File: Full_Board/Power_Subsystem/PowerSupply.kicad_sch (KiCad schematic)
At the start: 26 parts, among them IC4 LM2576HVS-5.0_NOPB, J7 KLDHCX-8-0202-A, U1 LM2576SX-3.3-NOPB

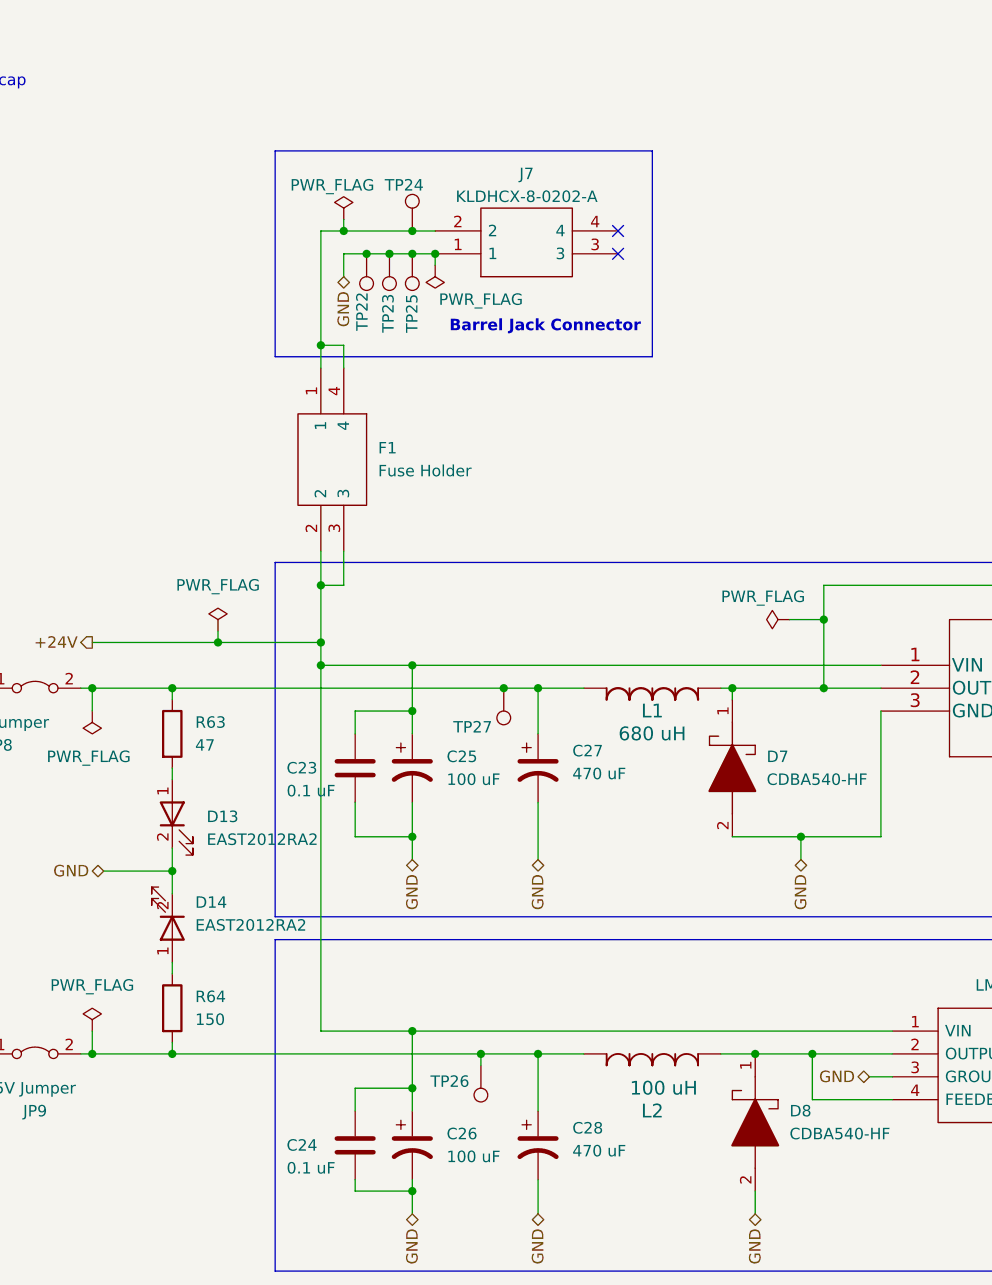
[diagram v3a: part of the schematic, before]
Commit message: Resolve misconfigured components, replace PCB from now completed schematic
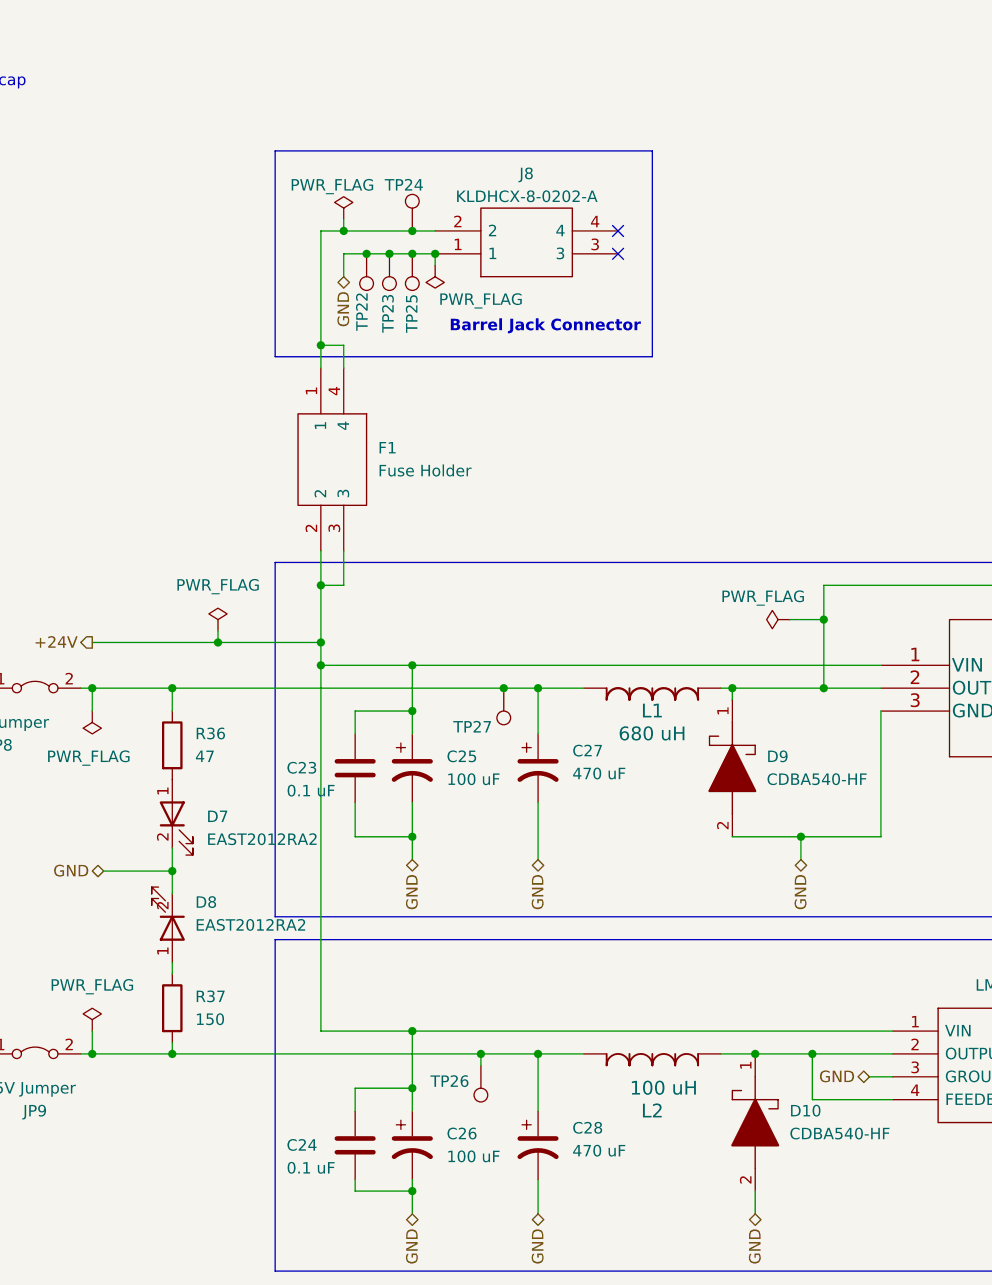
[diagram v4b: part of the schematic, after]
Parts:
- L2: footprint IND_44.104NLT_PUL -> PA4344-104NLT:PA4344.104NLT
- R36: renamed from R64; value 150 -> 47; footprint (none) -> CHP2512AFX-47R0ELF:RESC6431X130N; Digikey Part Number (none) -> 118-CHP2512AFX-47R0ELFCT-ND; Digikey link (none) -> https://www.digikey.com/en/products/detail/bourns-inc/CHP25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; Manufacturer's Part Number (none) -> CHP2512AFX-47R0ELF; Mouser Part Number (none) -> 652-CHP2512AFX-47R0L; Mouser link (none) -> https://www.mouser.com/ProductDetail/Bourns/CHP2512AFX-47R0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
- R37: renamed from R63; value 47 -> 150; footprint (none) -> SDR03EZPF1500:RESC1608X55N; Digikey Part Number (none) -> 511-SDR03EZPF1500CT-ND; Digikey link (none) -> https://www.digikey.com/en/products/detail/rohm-semiconduct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; Manufacturer's Part Number (none) -> SDR03EZPF1500; Mouser Part Number (none) -> 755-SDR03EZPF1500; Mouser link (none) -> https://www.mouser.com/ProductDetail/ROHM-Semiconductor/SDR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
- renumbered D8 to D10, D13 to D7, D14 to D8, D7 to D9, J7 to J8
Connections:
- net at C28.1, JP9.2 (B), L2.1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: now also R37.2; no longer R36.2
- net at D7.1: now also R36.2; no longer R37.2
- net at D8.1: now also R37.1; no longer R36.1
- net at C27.1, JP8.2 (B), L1.1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: now also R36.1; no longer R37.1
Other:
- moved on the sheet: R36, R37

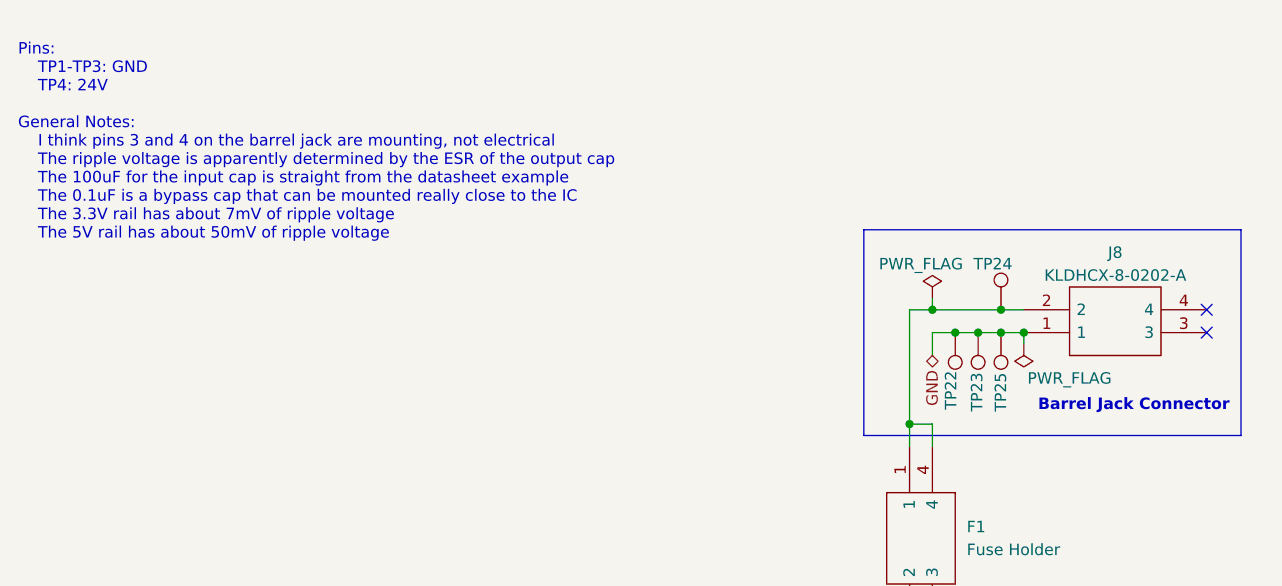
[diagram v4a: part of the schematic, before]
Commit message: Swapped pins on the barrel jack
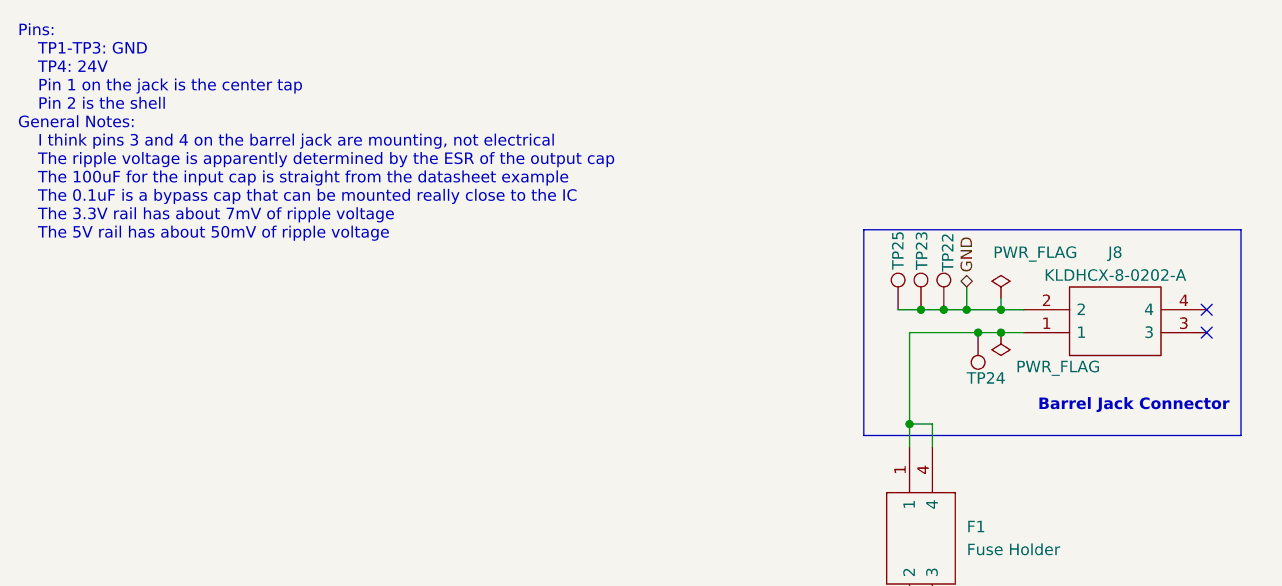
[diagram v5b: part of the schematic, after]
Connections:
- net GND: now also J8.2; no longer J8.1
- net at F1.1, F1.4, TP24.1: now also J8.1; no longer J8.2
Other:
- note added: "Pins: TP1-TP3: GND TP4: 24V Pin 1 on the jack is the center tap Pin 2 is the shell General Notes: I think pins 3 and 4 on the barrel jack are mounting, not electrical The ripple voltage is apparently determined by the ESR of the output cap The 100uF for the input cap is straight from the datasheet example The 0.1uF is a bypass cap that can be mounted really close to the IC The 3.3V rail has about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"
- note removed: "Pins: TP1-TP3: GND TP4: 24V General Notes: I think pins 3 and 4 on the barrel jack are mounting, not electrical The ripple voltage is apparently determined by the ESR of the output cap The 100uF for the input cap is straight from the datasheet example The 0.1uF is a bypass cap that can be mounted really close to the IC The 3.3V rail has about 7mV of ripple voltage The 5V rail has about 50mV of ri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"
- moved on the sheet: TP22, TP23, TP24, TP25
